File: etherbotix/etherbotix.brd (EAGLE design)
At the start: 100 x 50 mm, 111 parts, among them J1 J3011G21DNL, J10 JUMPER, J2 22-03-5035, J3 22-03-5035, J4 22-03-5045, J5 22-03-5045, J6 1760520000, J7 1760490000, J8 502443-0470, J9 502443-0470, T1 TESTPAD, T2 TESTPAD, T3 TESTPAD, T4 TESTPAD, T5 TESTPAD, T6 TESTPAD, T7 TESTPAD, T8 TESTPAD, T9 TESTPAD, U1 STM32F407V, U2 TLK110, U3 OKI-78SR-5, U4 TLV1117, U5 ACS711ELCTR-25AB-T, U6 ACS711ELCTR-25AB-T, U7 MAX481CSA, U8 74LS126D, X1 25MHZ

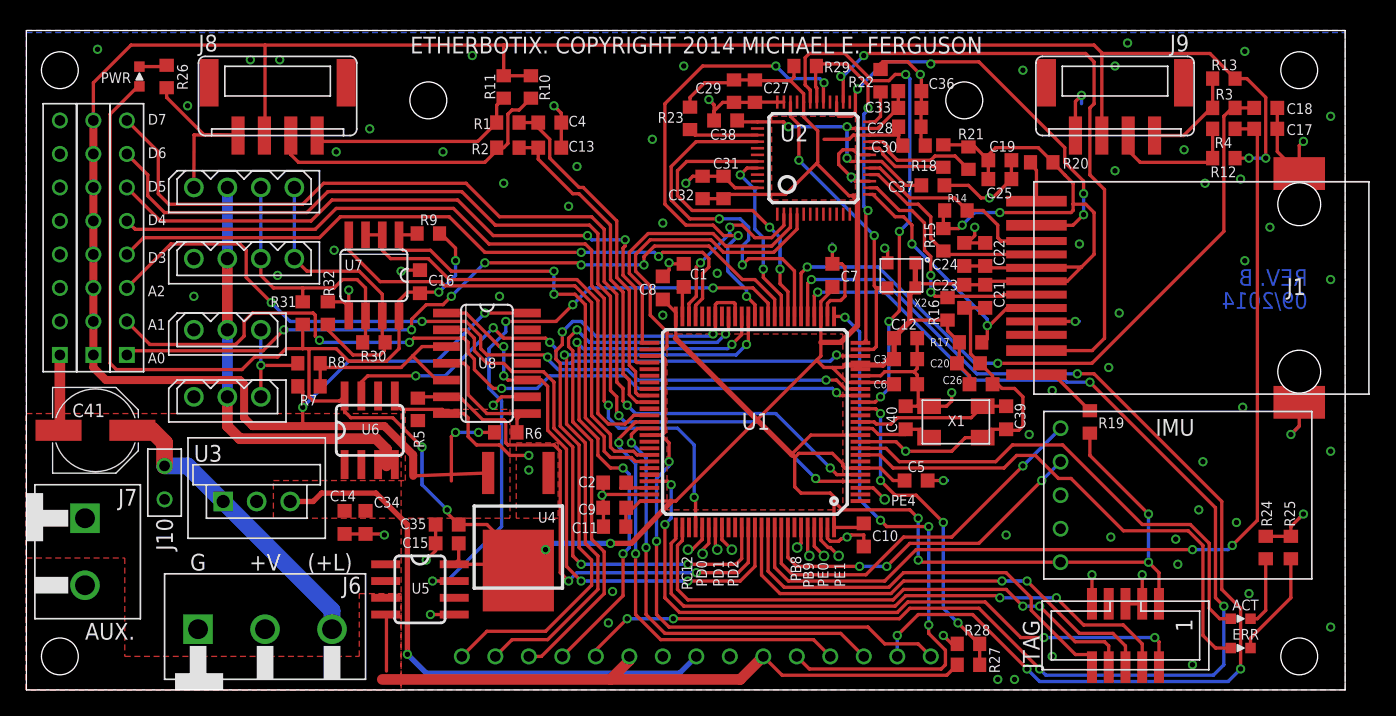
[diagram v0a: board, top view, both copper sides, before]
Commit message: add testpads to clocks, encoders, current sense
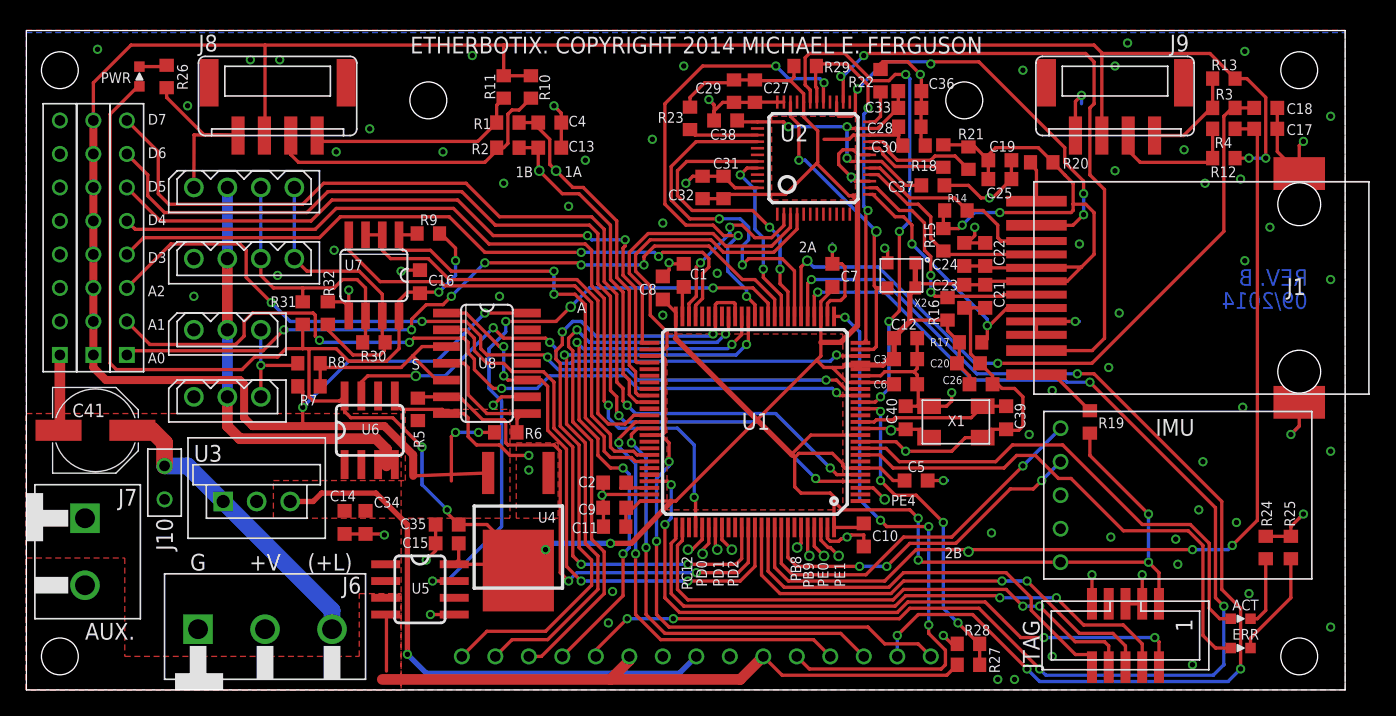
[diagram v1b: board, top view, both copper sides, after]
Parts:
- added T10, T11, T12, T13, T14, T15, T16, T17: TESTPAD, fergs:TEST
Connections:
- net AUX_CURRENT_SENSE: now also T17.T
- net ETH_CLK: now also T10.T
- net M1_ENC_A: now also T12.T
- net M1_ENC_B: now also T13.T
- net M2_ENC_A: now also T14.T
- net M2_ENC_B: now also T15.T
- net N$15: now also T11.T
- net SERVO_CURRENT_SENSE: now also T16.T
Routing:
- net N$15: track 6.63 -> 5.56 mm
- net M2_ENC_A: track 54.0 -> 54.7 mm, vias 2 -> 1
- net ETH_CLK: track 24.2 -> 24.6 mm, vias 2 -> 1
- net AUX_CURRENT_SENSE: vias 4 -> 3
- net SERVO_CURRENT_SENSE: vias 4 -> 3
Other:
- board text added: "1A"
- board text added: "1B"
- board text added: "2A"
- board text added: "2B"
- board text added: "A"
- board text added: "S"

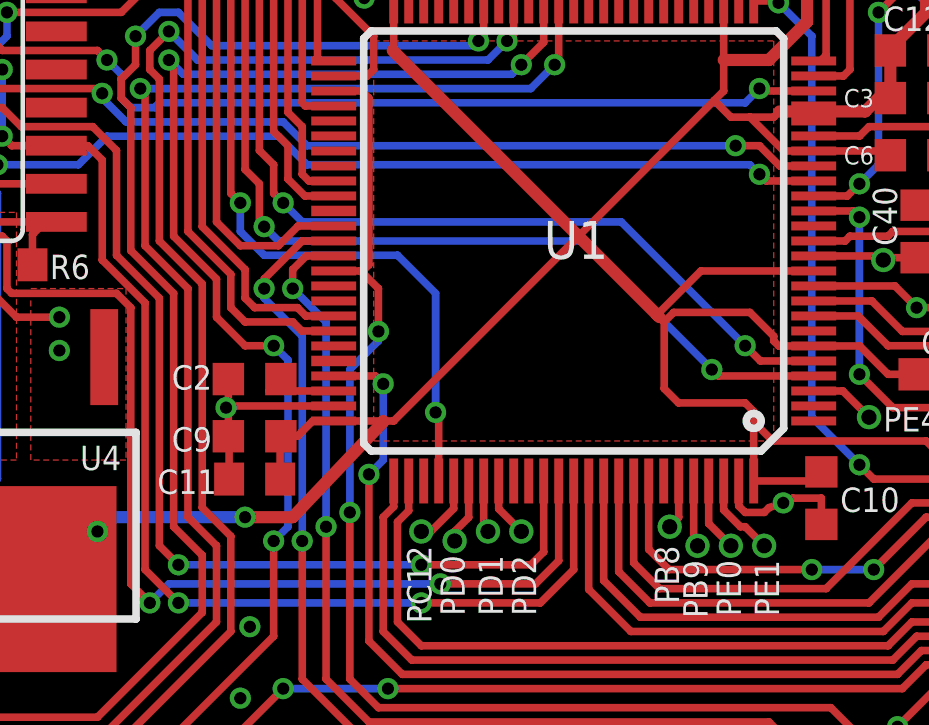
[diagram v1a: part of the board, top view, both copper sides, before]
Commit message: add testpad for PA8 (mco1)
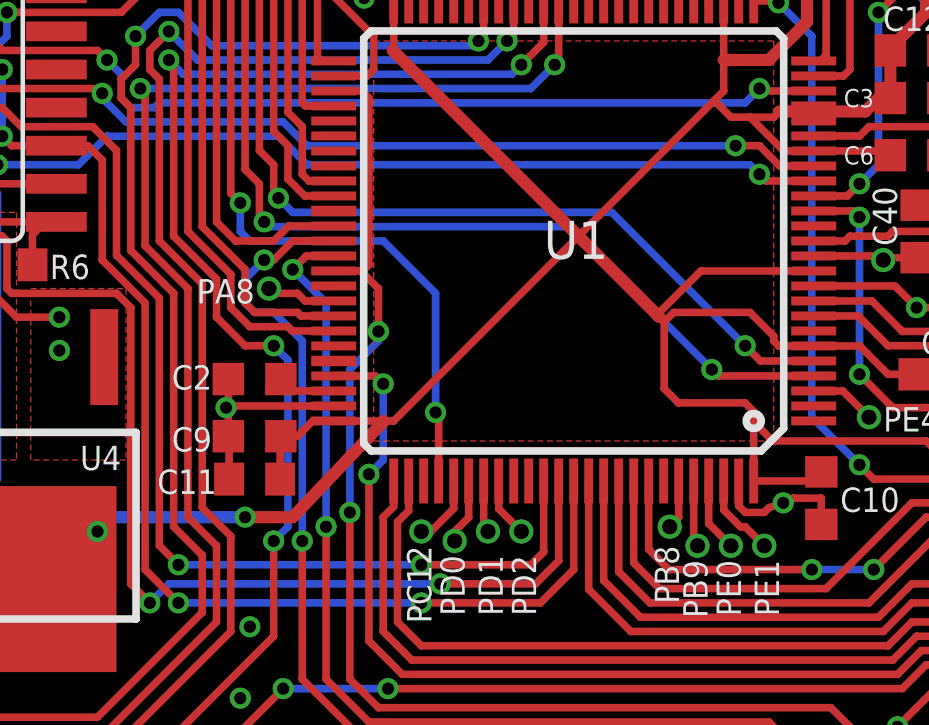
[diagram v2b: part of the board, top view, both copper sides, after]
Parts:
- added T18: TESTPAD, fergs:TEST
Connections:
- new net PA8: T18.T, U1.67
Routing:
- net PA8: track 0.00 -> 2.33 mm
- net M2_PWM: track 32.8 -> 34.1 mm
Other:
- board text added: "PA8"

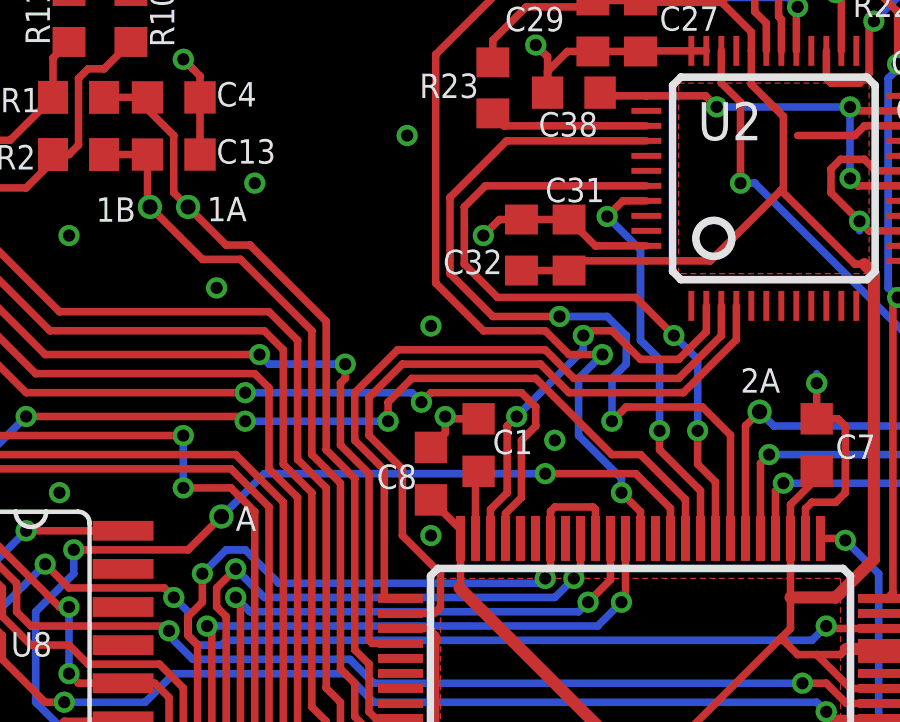
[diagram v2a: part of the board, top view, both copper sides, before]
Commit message: add pin to force staying in bootloader
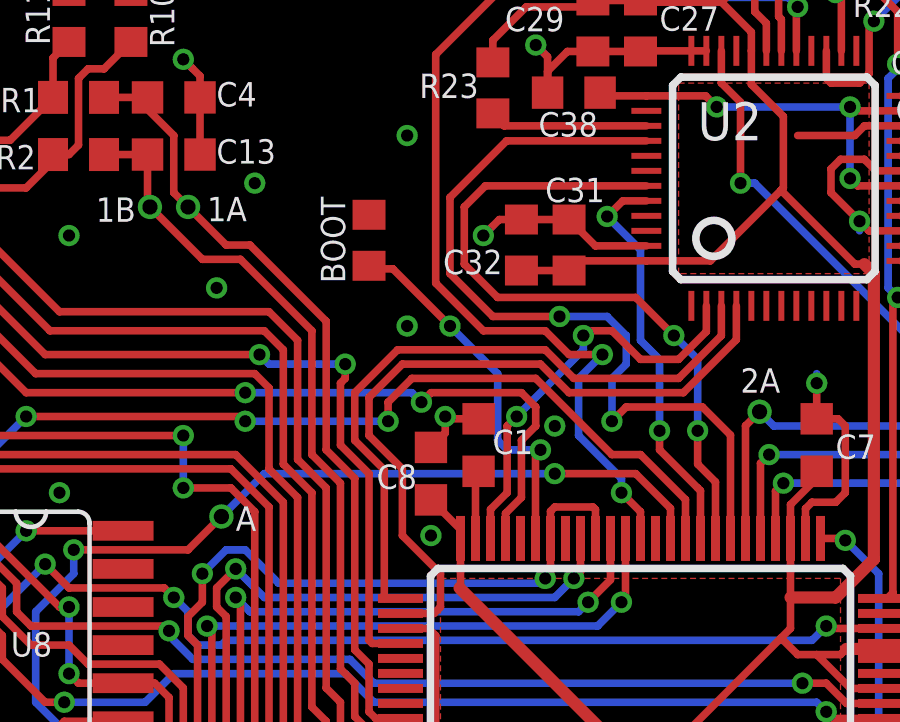
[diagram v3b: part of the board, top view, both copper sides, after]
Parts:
- added BOOT: DNS, fergs:0603
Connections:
- new net FORCE_BOOTLOADER: BOOT.1, U1.45
- net GND: now also BOOT.2
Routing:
- net FORCE_BOOTLOADER: track 0.00 -> 12.6 mm, vias 0 -> 2
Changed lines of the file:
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@@
 <element name="T17" library="fergs" package="TEST" value="TESTPAD" x="41.275" y="29.05125"/>
 <element name="T18" library="fergs" package="TEST" value="TESTPAD" x="45.085" y="18.7325"/>
+<element name="BOOT" library="fergs" package="0603" value="DNS" x="46.19625" y="38.25875" smashed="yes" rot="R90">
+<attribute name="NAME" x="45.4025" y="36.83" size="0.8128" layer="25" rot="R90"/>
+<attribute name="VALUE" x="48.10125" y="37.62375" size="1.27" layer="27" rot="R90"/>
+</element>
 </elements>
 <signals>
@@
 <via x="83.5025" y="49.05375" extent="1-16" drill="0.4064"/>
 <via x="49.8475" y="47.3075" extent="1-16" drill="0.4064"/>
-<via x="48.26" y="35.40125" extent="1-16" drill="0.4064"/>
+<via x="47.46625" y="35.40125" extent="1-16" drill="0.4064"/>
 <via x="42.38625" y="40.16375" extent="1-16" drill="0.4064"/>
 <via x="26.035" y="42.545" extent="1-16" drill="0.4064"/>
@@
 <via x="35.8775" y="29.845" extent="1-16" drill="0.4064"/>
 <via x="48.26" y="28.41625" extent="1-16" drill="0.4064"/>
-<via x="52.3875" y="31.59125" extent="1-16" drill="0.4064"/>
+<via x="52.3875" y="32.0675" extent="1-16" drill="0.4064"/>
 <via x="23.495" y="40.79875" extent="1-16" drill="0.4064"/>
 <via x="31.59125" y="40.79875" extent="1-16" drill="0.4064"/>
@@
 <via x="76.04125" y="19.3675" extent="1-16" drill="0.4064"/>
 <via x="19.05" y="31.4325" extent="1-16" drill="0.4064"/>
+<contactref element="BOOT" pad="2"/>
 </signal>
 <signal name="+5V">
@@
 <wire x1="56.245" y1="28.32" x2="56.245" y2="29.32125" width="0.254" layer="1"/>
 <wire x1="56.245" y1="29.32125" x2="55.08625" y2="30.48" width="0.254" layer="1"/>
-<wire x1="55.08625" y1="30.48" x2="52.07" y2="30.48" width="0.254" layer="1"/>
-<via x="52.07" y="30.48" extent="1-16" drill="0.4064"/>
-<wire x1="52.07" y1="30.48" x2="42.70375" y2="30.48" width="0.254" layer="16"/>
+<wire x1="55.08625" y1="30.48" x2="52.3875" y2="30.48" width="0.254" layer="1"/>
+<via x="52.3875" y="30.48" extent="1-16" drill="0.4064"/>
+<wire x1="52.3875" y1="30.48" x2="42.70375" y2="30.48" width="0.254" layer="16"/>
 <wire x1="42.70375" y1="30.48" x2="41.275" y2="29.05125" width="0.254" layer="16"/>
 <wire x1="40.16375" y1="27.94" x2="36.35375" y2="27.94" width="0.254" layer="1"/>
@@
 <wire x1="45.24375" y1="18.57375" x2="45.085" y2="18.7325" width="0.254" layer="1"/>
 </signal>
+<signal name="FORCE_BOOTLOADER">
+<contactref element="U1" pad="45"/>
+<contactref element="BOOT" pad="1"/>
+<wire x1="51.745" y1="28.32" x2="51.745" y2="31.1075" width="0.254" layer="1"/>
+<wire x1="51.745" y1="31.1075" x2="51.91125" y2="31.27375" width="0.254" layer="1"/>
+<via x="51.91125" y="31.27375" extent="1-16" drill="0.4064"/>
+<wire x1="51.91125" y1="31.27375" x2="50.8" y2="31.27375" width="0.254" layer="16"/>
+<wire x1="50.8" y1="31.27375" x2="50.4825" y2="31.59125" width="0.254" layer="16"/>
+<wire x1="50.4825" y1="31.59125" x2="50.4825" y2="33.81375" width="0.254" layer="16"/>
+<wire x1="50.4825" y1="33.81375" x2="48.895" y2="35.40125" width="0.254" layer="16"/>
+<via x="48.895" y="35.40125" extent="1-16" drill="0.4064"/>
+<wire x1="48.895" y1="35.40125" x2="46.99" y2="37.30625" width="0.254" layer="1"/>
+<wire x1="46.99" y1="37.30625" x2="46.29875" y2="37.30625" width="0.254" layer="1"/>
+<wire x1="46.29875" y1="37.30625" x2="46.19625" y2="37.40875" width="0.254" layer="1"/>
+</signal>
 </signals>
